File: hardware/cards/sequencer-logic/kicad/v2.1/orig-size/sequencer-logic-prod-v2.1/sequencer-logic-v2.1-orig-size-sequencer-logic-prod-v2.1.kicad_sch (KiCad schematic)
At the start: 0 parts

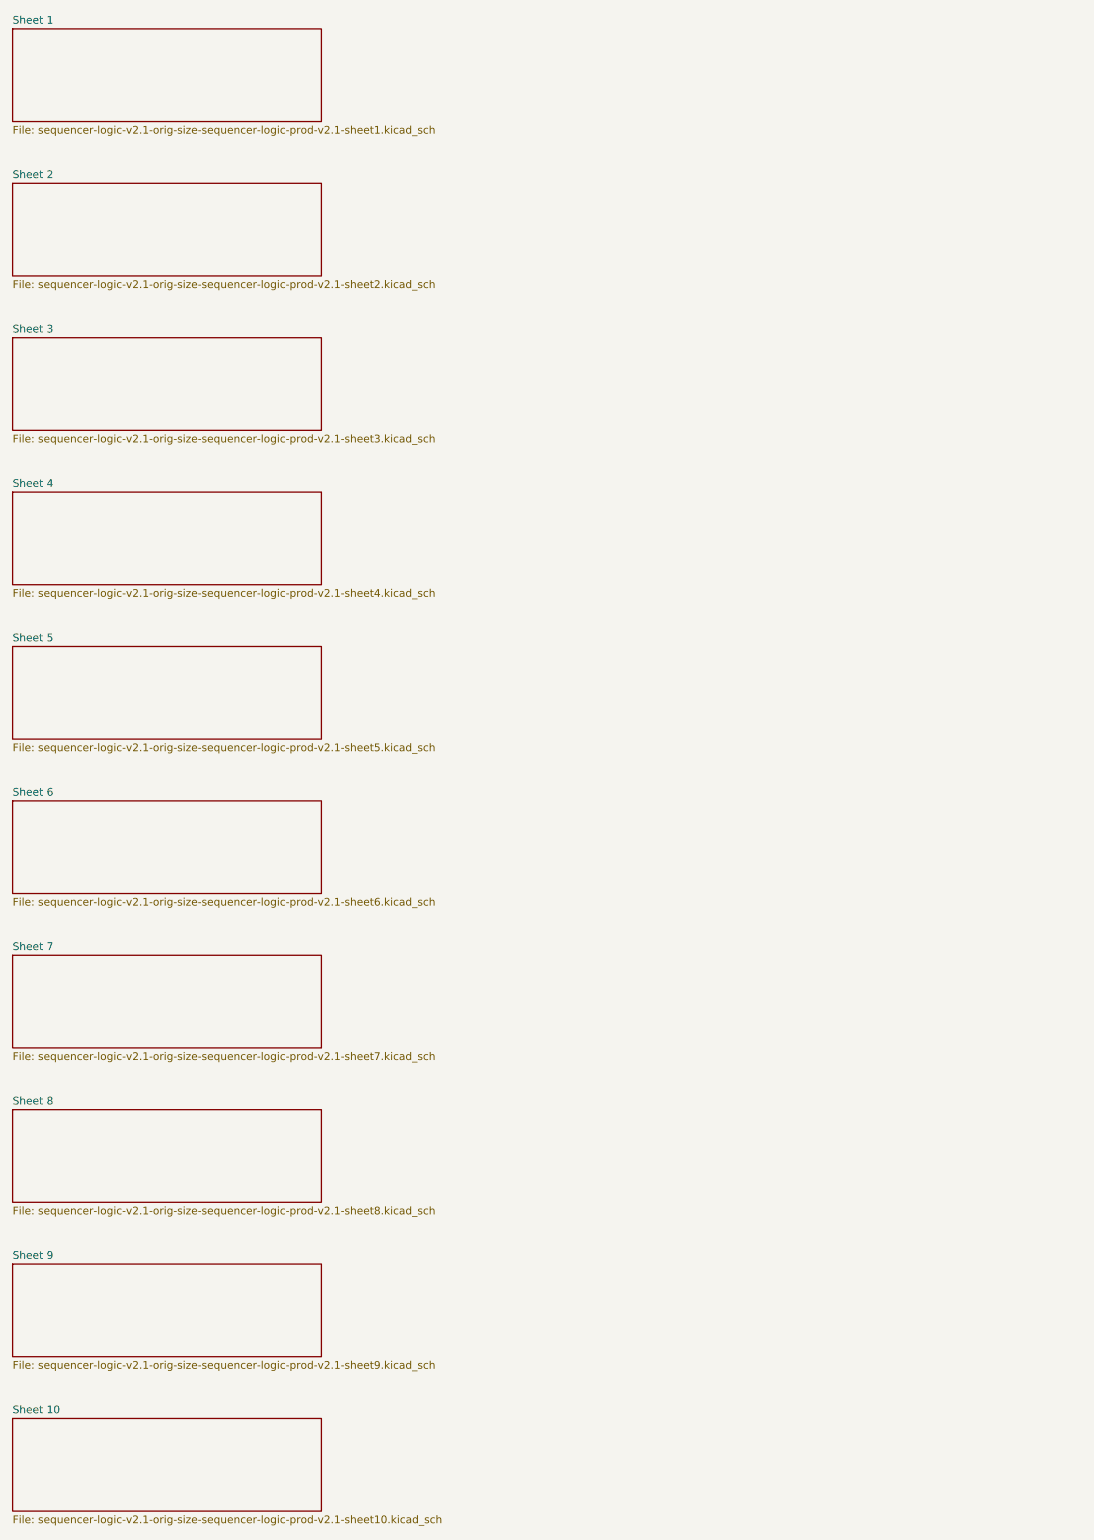
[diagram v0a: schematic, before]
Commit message: fix(kicad): readable converted schematics - overlaps 42,847 -> 3,147, nothing off the frame; CF sheet 0 overlaps
- tools/kicad/sch_overlaps.py: calibrated readability check (text/text, text/body, text/line, off frame/title block)
- eagle_sch_to_kicad.py: fields placed from Eagle's smashed attributes or the symbol's >NAME/>VALUE with Eagle's align,
  size and ratio, readable angles; fields Eagle never shows hidden (FABC96R shows only its pin name); pin numbers hidden
  where every Eagle pin hides them; Eagle-hidden layers dropped (the stray SpiceOrder text); labels on their own wires,
  converter labels only where KiCad needs them; rotate-then-mirror fixed for MR90/MR270 in pin_world/no-connects;
  each sheet on the smallest page that holds it, centred clear of the title block
- finish_board.py: stable footprint-library choice (DRC counts no longer vary run to run)
- all 37 projects regenerated: netlist proofs unchanged (34 MATCH, 2 schematic-only, video Fusion export MISMATCH as
  before); DRC same or better; ERC up (loose wire ends onto graphic buses no longer hidden by labels; explained per README)
- CF card: gate names off the gate bodies, U3 clear of its title, 5.08 mm connector pins; rebuilt: DRC 0/0, proof MATCH
- schematic PDFs regenerated (tools/sch_to_pdf.py, 37/37)

Co-Authored-By: Claude Opus 5.5 <noreply@anthropic.com>
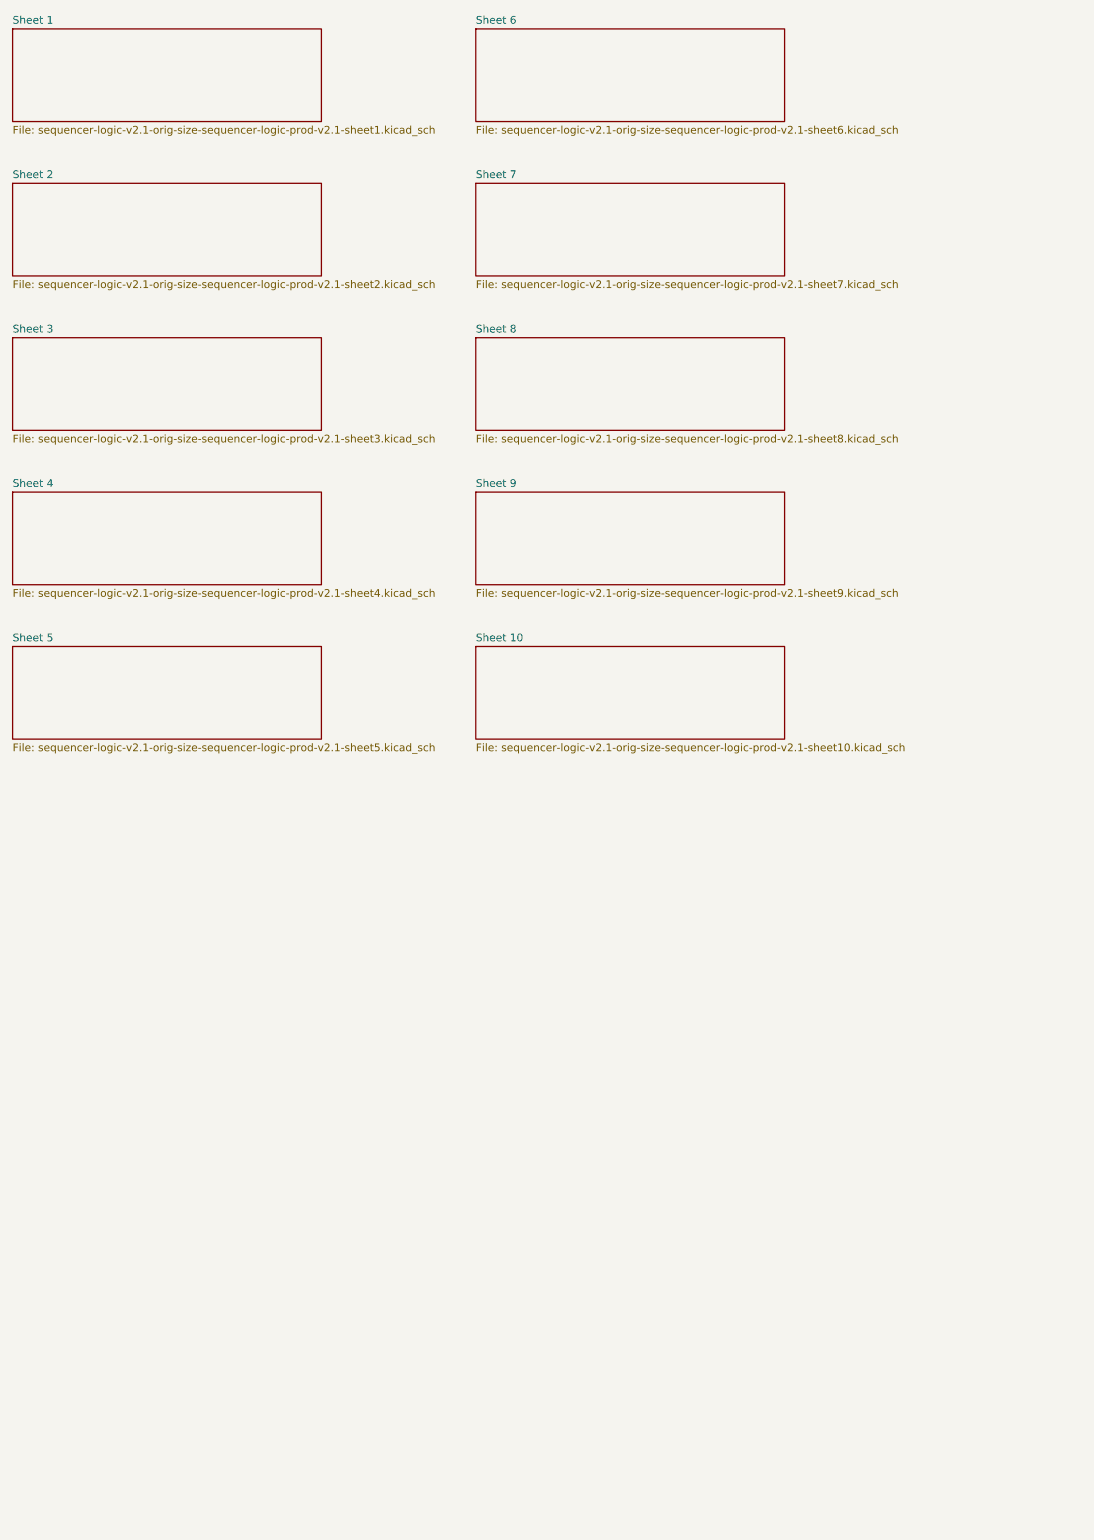
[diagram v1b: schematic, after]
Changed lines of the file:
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@@
 		(instances (project "sequencer-logic-v2.1-orig-size-sequencer-logic-prod-v2.1" (path "/9262d55c-b2cf-22ab-70ce-4a318e710945" (page "6"))))
 	)
-	(sheet (at 25.4 152.4) (size 50.8 15.24) (exclude_from_sim no) (in_bom yes) (on_board yes) (dnp no) (fields_autoplaced yes)
+	(sheet (at 101.6 25.4) (size 50.8 15.24) (exclude_from_sim no) (in_bom yes) (on_board yes) (dnp no) (fields_autoplaced yes)
 		(stroke (width 0.1524) (type solid)) (fill (color 0 0 0 0.0))
-		(property "Sheetname" "Sheet 6" (at 25.4 151.7 0) (effects (font (size 1.27 1.27)) (justify left bottom)))
-		(property "Sheetfile" "sequencer-logic-v2.1-orig-size-sequencer-logic-prod-v2.1-sheet6.kicad_sch" (at 25.4 168.3 0) (effects (font (size 1.27 1.27)) (justify left top)))
+		(property "Sheetname" "Sheet 6" (at 101.6 24.7 0) (effects (font (size 1.27 1.27)) (justify left bottom)))
+		(property "Sheetfile" "sequencer-logic-v2.1-orig-size-sequencer-logic-prod-v2.1-sheet6.kicad_sch" (at 101.6 41.3 0) (effects (font (size 1.27 1.27)) (justify left top)))
 		(instances (project "sequencer-logic-v2.1-orig-size-sequencer-logic-prod-v2.1" (path "/9262d55c-b2cf-22ab-70ce-4a318e710945" (page "7"))))
 	)
-	(sheet (at 25.4 177.8) (size 50.8 15.24) (exclude_from_sim no) (in_bom yes) (on_board yes) (dnp no) (fields_autoplaced yes)
+	(sheet (at 101.6 50.8) (size 50.8 15.24) (exclude_from_sim no) (in_bom yes) (on_board yes) (dnp no) (fields_autoplaced yes)
 		(stroke (width 0.1524) (type solid)) (fill (color 0 0 0 0.0))
-		(property "Sheetname" "Sheet 7" (at 25.4 177.1 0) (effects (font (size 1.27 1.27)) (justify left bottom)))
-		(property "Sheetfile" "sequencer-logic-v2.1-orig-size-sequencer-logic-prod-v2.1-sheet7.kicad_sch" (at 25.4 193.7 0) (effects (font (size 1.27 1.27)) (justify left top)))
+		(property "Sheetname" "Sheet 7" (at 101.6 50.1 0) (effects (font (size 1.27 1.27)) (justify left bottom)))
+		(property "Sheetfile" "sequencer-logic-v2.1-orig-size-sequencer-logic-prod-v2.1-sheet7.kicad_sch" (at 101.6 66.7 0) (effects (font (size 1.27 1.27)) (justify left top)))
 		(instances (project "sequencer-logic-v2.1-orig-size-sequencer-logic-prod-v2.1" (path "/9262d55c-b2cf-22ab-70ce-4a318e710945" (page "8"))))
 	)
-	(sheet (at 25.4 203.2) (size 50.8 15.24) (exclude_from_sim no) (in_bom yes) (on_board yes) (dnp no) (fields_autoplaced yes)
+	(sheet (at 101.6 76.2) (size 50.8 15.24) (exclude_from_sim no) (in_bom yes) (on_board yes) (dnp no) (fields_autoplaced yes)
 		(stroke (width 0.1524) (type solid)) (fill (color 0 0 0 0.0))
-		(property "Sheetname" "Sheet 8" (at 25.4 202.5 0) (effects (font (size 1.27 1.27)) (justify left bottom)))
-		(property "Sheetfile" "sequencer-logic-v2.1-orig-size-sequencer-logic-prod-v2.1-sheet8.kicad_sch" (at 25.4 219.1 0) (effects (font (size 1.27 1.27)) (justify left top)))
+		(property "Sheetname" "Sheet 8" (at 101.6 75.5 0) (effects (font (size 1.27 1.27)) (justify left bottom)))
+		(property "Sheetfile" "sequencer-logic-v2.1-orig-size-sequencer-logic-prod-v2.1-sheet8.kicad_sch" (at 101.6 92.1 0) (effects (font (size 1.27 1.27)) (justify left top)))
 		(instances (project "sequencer-logic-v2.1-orig-size-sequencer-logic-prod-v2.1" (path "/9262d55c-b2cf-22ab-70ce-4a318e710945" (page "9"))))
 	)
-	(sheet (at 25.4 228.6) (size 50.8 15.24) (exclude_from_sim no) (in_bom yes) (on_board yes) (dnp no) (fields_autoplaced yes)
+	(sheet (at 101.6 101.6) (size 50.8 15.24) (exclude_from_sim no) (in_bom yes) (on_board yes) (dnp no) (fields_autoplaced yes)
 		(stroke (width 0.1524) (type solid)) (fill (color 0 0 0 0.0))
-		(property "Sheetname" "Sheet 9" (at 25.4 227.9 0) (effects (font (size 1.27 1.27)) (justify left bottom)))
-		(property "Sheetfile" "sequencer-logic-v2.1-orig-size-sequencer-logic-prod-v2.1-sheet9.kicad_sch" (at 25.4 244.5 0) (effects (font (size 1.27 1.27)) (justify left top)))
+		(property "Sheetname" "Sheet 9" (at 101.6 100.9 0) (effects (font (size 1.27 1.27)) (justify left bottom)))
+		(property "Sheetfile" "sequencer-logic-v2.1-orig-size-sequencer-logic-prod-v2.1-sheet9.kicad_sch" (at 101.6 117.5 0) (effects (font (size 1.27 1.27)) (justify left top)))
 		(instances (project "sequencer-logic-v2.1-orig-size-sequencer-logic-prod-v2.1" (path "/9262d55c-b2cf-22ab-70ce-4a318e710945" (page "10"))))
 	)
-	(sheet (at 25.4 254) (size 50.8 15.24) (exclude_from_sim no) (in_bom yes) (on_board yes) (dnp no) (fields_autoplaced yes)
+	(sheet (at 101.6 127) (size 50.8 15.24) (exclude_from_sim no) (in_bom yes) (on_board yes) (dnp no) (fields_autoplaced yes)
 		(stroke (width 0.1524) (type solid)) (fill (color 0 0 0 0.0))
-		(property "Sheetname" "Sheet 10" (at 25.4 253.3 0) (effects (font (size 1.27 1.27)) (justify left bottom)))
-		(property "Sheetfile" "sequencer-logic-v2.1-orig-size-sequencer-logic-prod-v2.1-sheet10.kicad_sch" (at 25.4 269.9 0) (effects (font (size 1.27 1.27)) (justify left top)))
+		(property "Sheetname" "Sheet 10" (at 101.6 126.3 0) (effects (font (size 1.27 1.27)) (justify left bottom)))
+		(property "Sheetfile" "sequencer-logic-v2.1-orig-size-sequencer-logic-prod-v2.1-sheet10.kicad_sch" (at 101.6 142.9 0) (effects (font (size 1.27 1.27)) (justify left top)))
 		(instances (project "sequencer-logic-v2.1-orig-size-sequencer-logic-prod-v2.1" (path "/9262d55c-b2cf-22ab-70ce-4a318e710945" (page "11"))))
 	)
